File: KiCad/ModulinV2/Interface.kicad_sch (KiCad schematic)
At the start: 69 parts, among them IC10 ADS7866IDBVT, IC11 DAC60501ZDGSR, IC12 DAC60501ZDGSR, IC4 TL072HIDR, IC5 TL072HIDR, IC6 TL074HIDR, IC7 ADS7041IDCUR, IC8 ADS7041IDCUR, IC9 ADS7866IDBVT

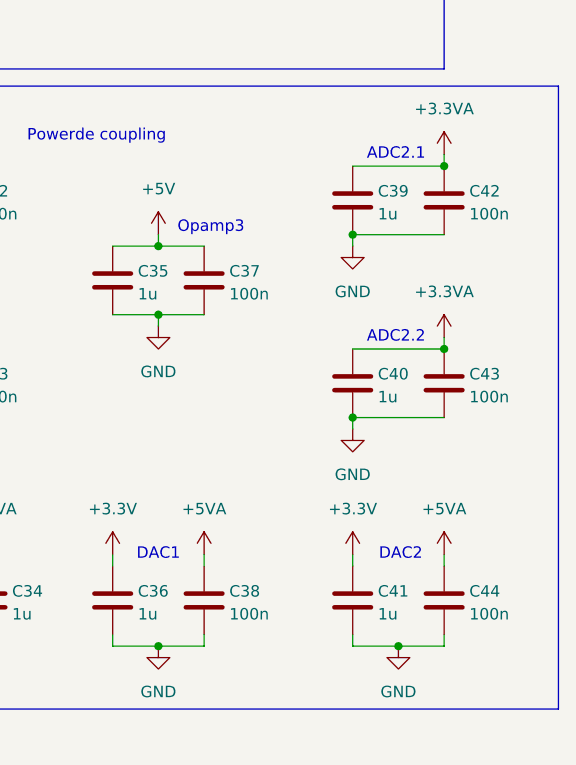
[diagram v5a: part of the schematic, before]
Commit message: Layed out Interface and PWR components and started with MCU layout
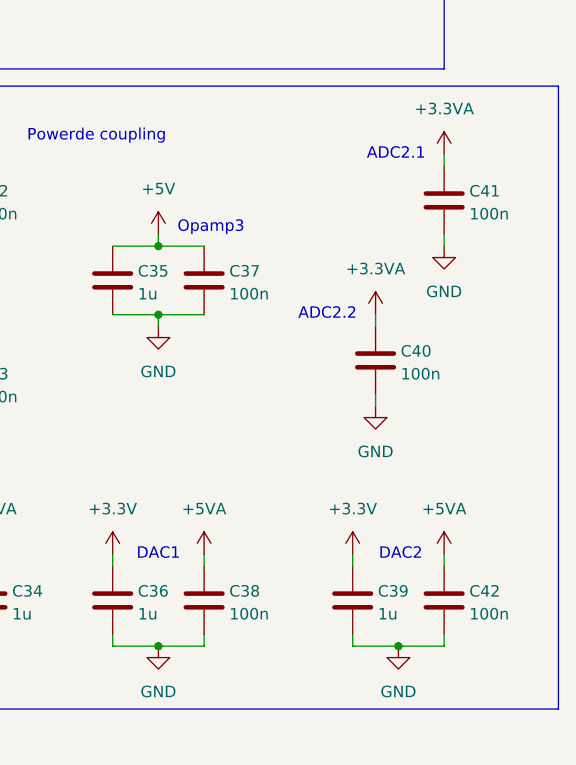
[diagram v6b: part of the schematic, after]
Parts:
- removed C39, C40: 1u, Capacitor_SMD:C_0603_1608Metric_Pad1.08x0.95mm_HandSolder, symbol Device:C
- renumbered C41 to C39, C43 to C40, C42 to C41, C44 to C42
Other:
- moved on the sheet: C40

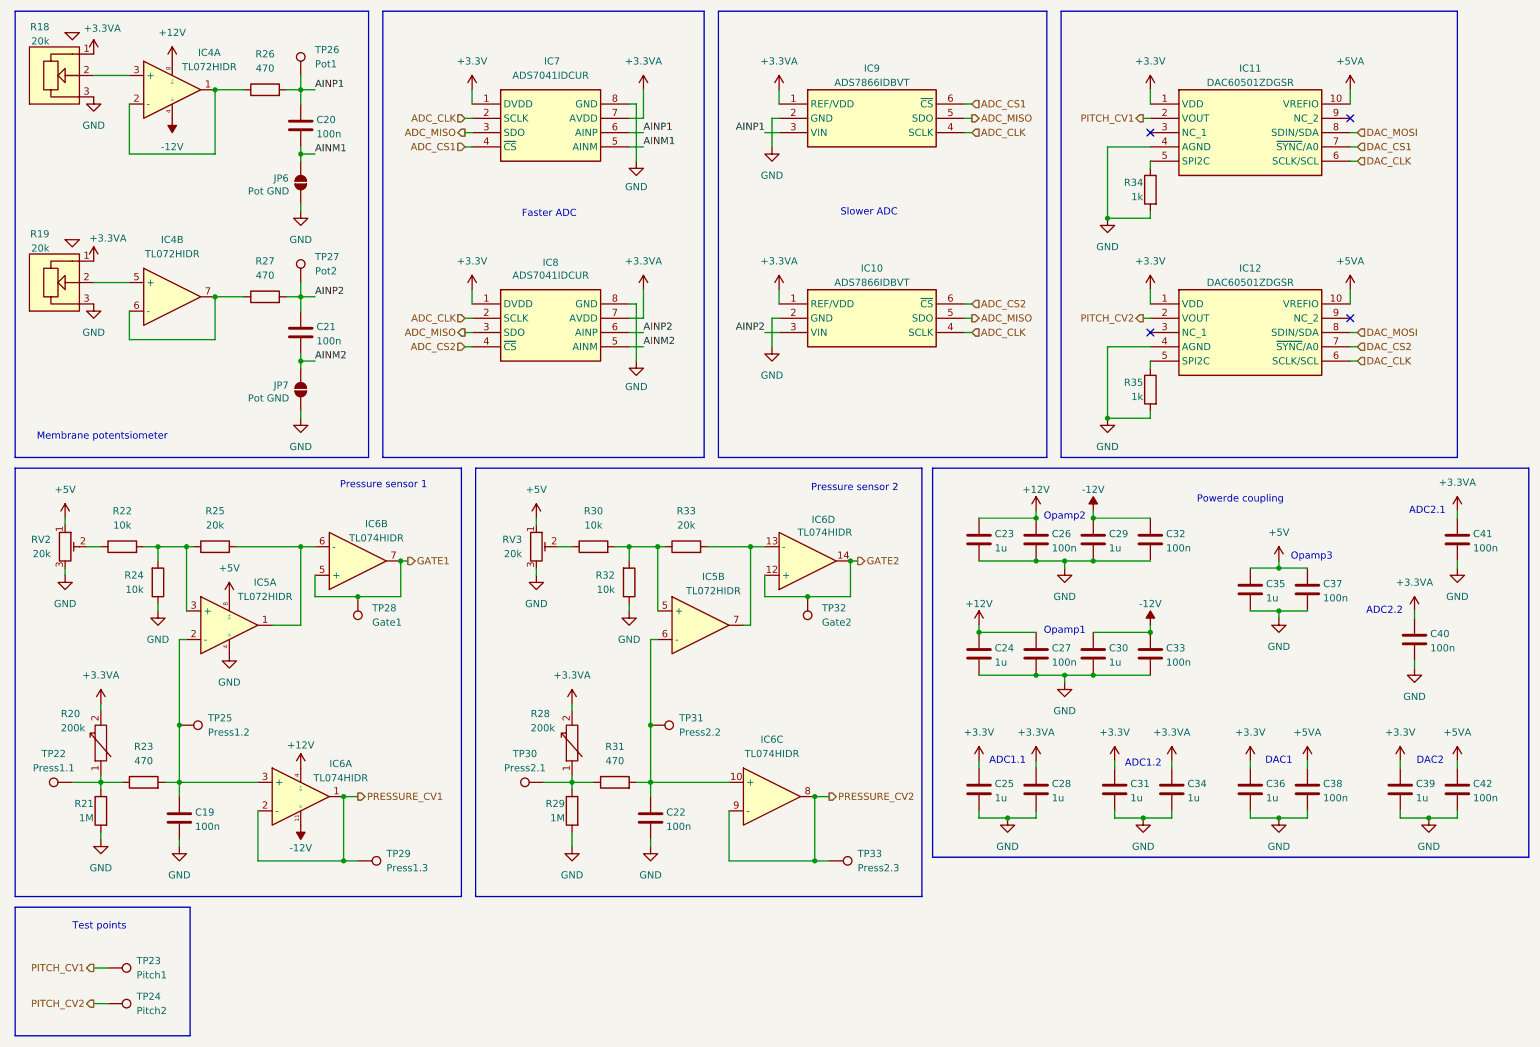
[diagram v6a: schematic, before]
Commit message: Completed tuning & mod wheel layouts
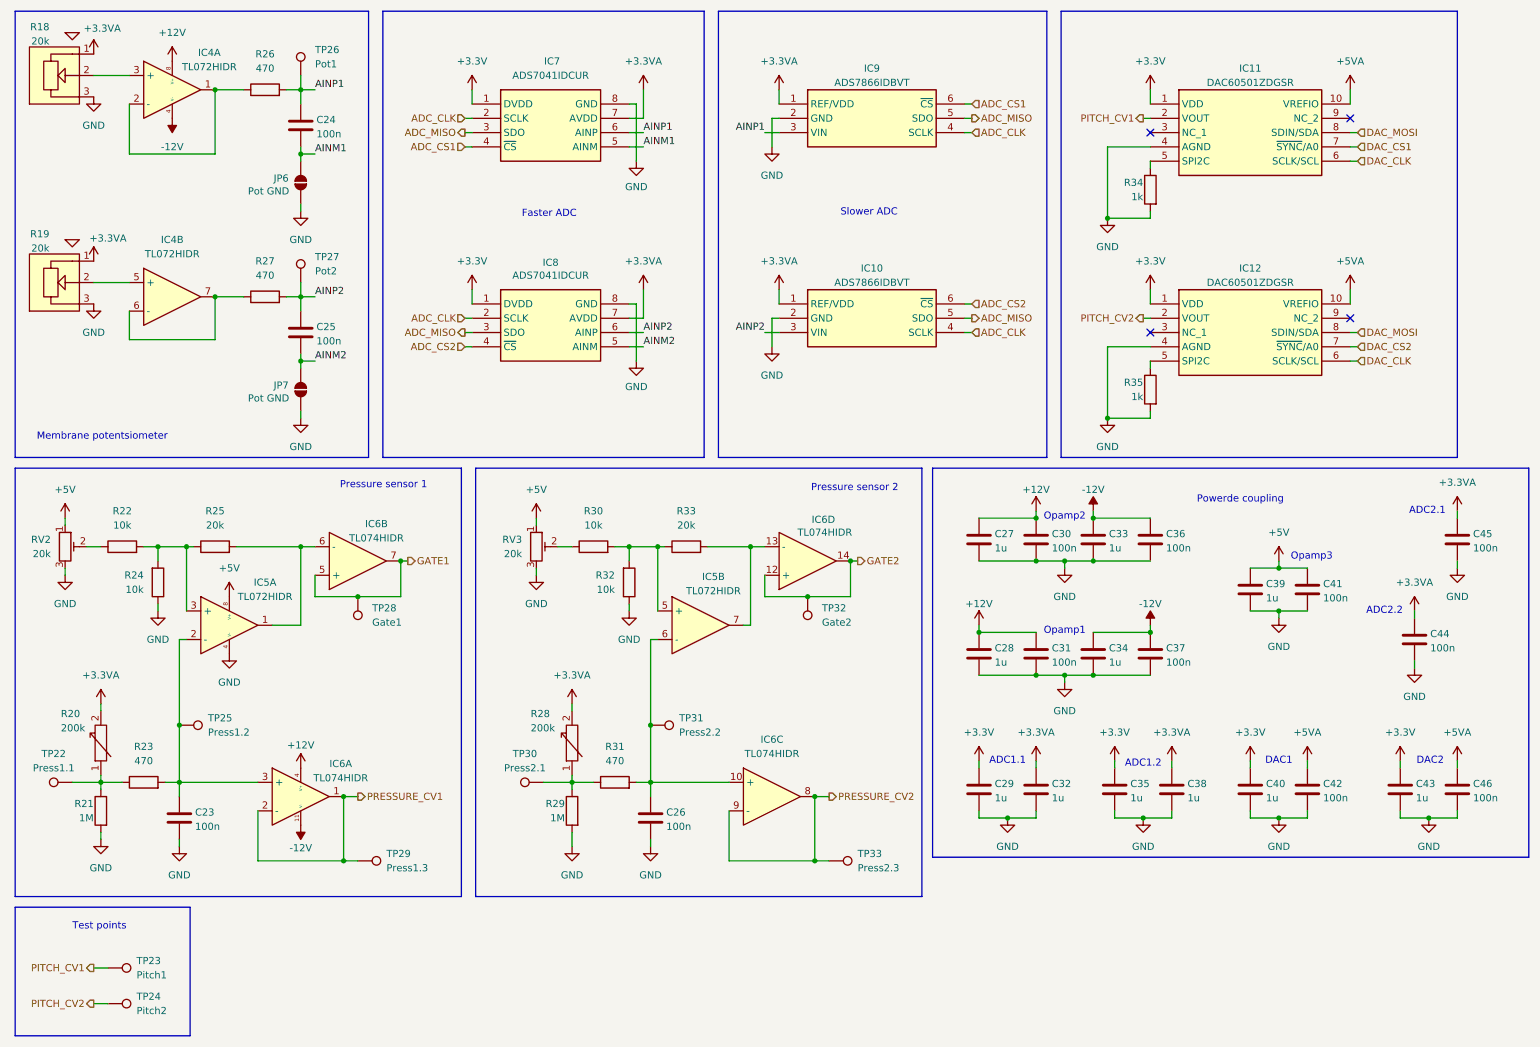
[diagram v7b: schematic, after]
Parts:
- renumbered C19 to C23, C20 to C24, C21 to C25, C22 to C26, C23 to C27, C24 to C28, C25 to C29, C26 to C30, C27 to C31, C28 to C32, C29 to C33, C30 to C34, C31 to C35, C32 to C36, C33 to C37, C34 to C38, C35 to C39, C36 to C40, C37 to C41, C38 to C42, C39 to C43, C40 to C44, C41 to C45, C42 to C46
